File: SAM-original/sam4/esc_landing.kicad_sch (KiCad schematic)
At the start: 14 parts, among them J1 MR30PW-FB, J2 MR30PW-FB, J3 MR30PW-FB, J4 MR30PW-FB, U1 BM10B-SRSS-TB, U2 T-motor_F55A_PROII

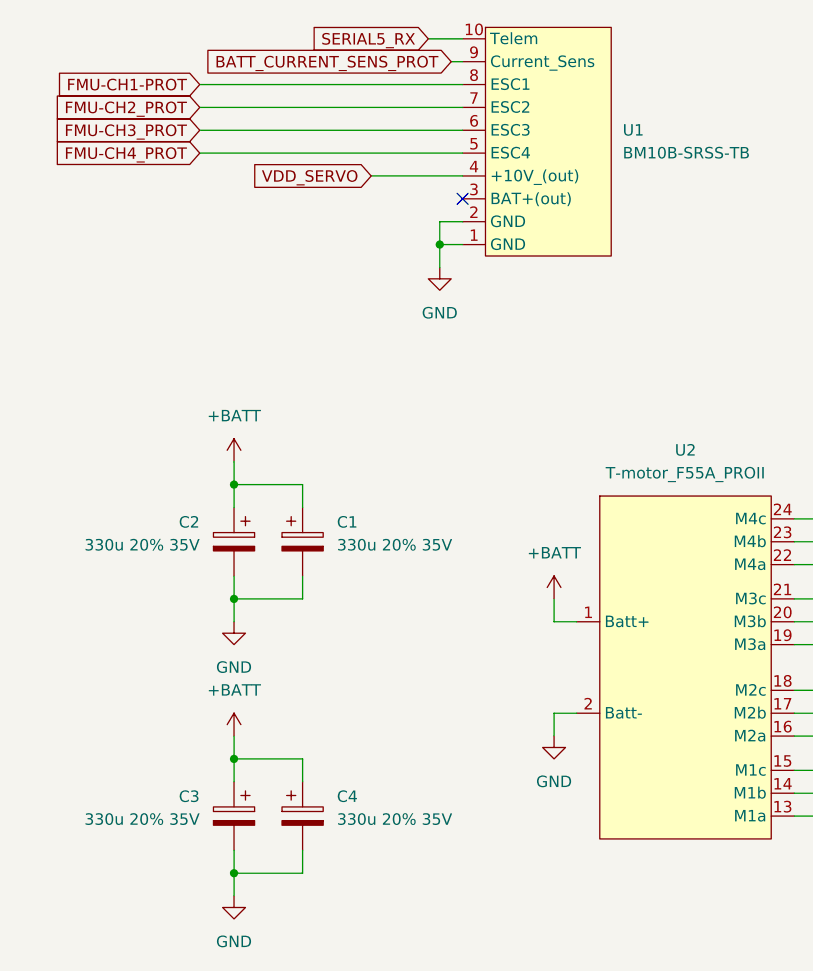
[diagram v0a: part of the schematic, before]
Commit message: reannotate sam schem to bring into parity
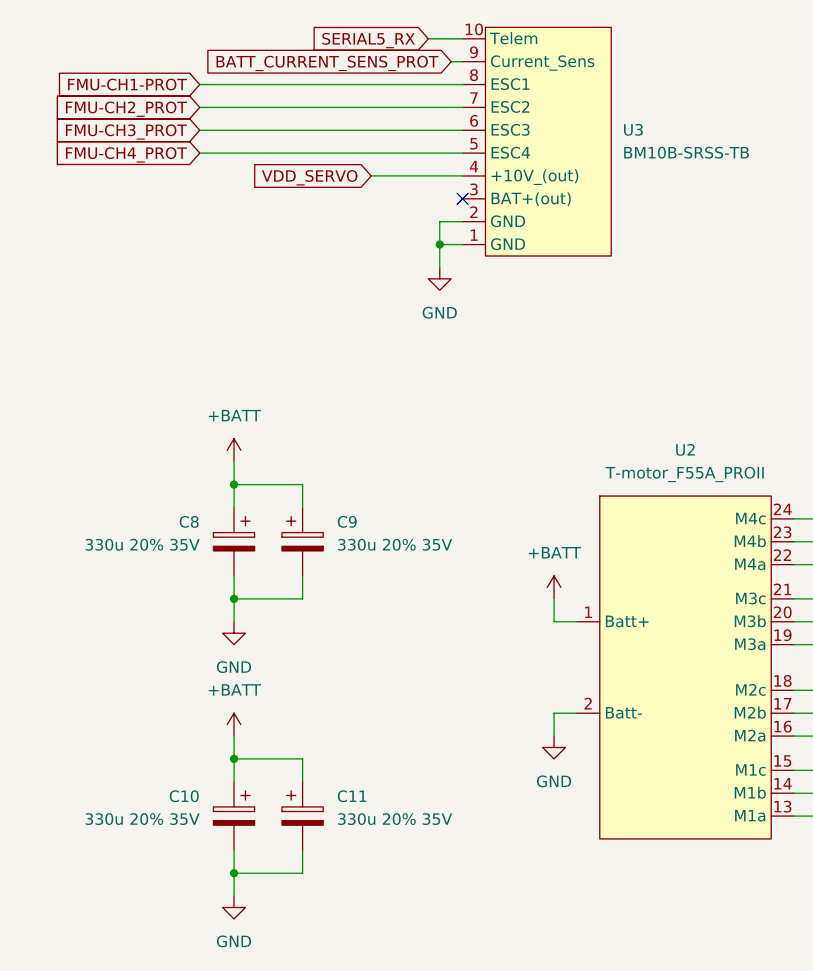
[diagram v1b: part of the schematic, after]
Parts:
- renumbered C3 to C10, C4 to C11, C2 to C8, C1 to C9, U1 to U3
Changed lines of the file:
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@@
 		(on_board yes)
 		(dnp no)
-		(property "Reference" "C3"
+		(property "Reference" "C10"
 			(at 44.45 112.1409 0)
 			(effects
@@
 			(project "sam4"
 				(path "/01aa8038-f16d-42dc-9377-7a3d64116781/45b0968d-ea93-472f-9fa5-36e57b913607"
-					(reference "C3")
+					(reference "C10")
 					(unit 1)
 				)
@@
 		(dnp no)
 		(fields_autoplaced yes)
-		(property "Reference" "C1"
+		(property "Reference" "C9"
 			(at 59.69 81.6609 0)
 			(effects
@@
 			(project ""
 				(path "/01aa8038-f16d-42dc-9377-7a3d64116781/45b0968d-ea93-472f-9fa5-36e57b913607"
-					(reference "C1")
+					(reference "C9")
 					(unit 1)
 				)
@@
 		(dnp no)
 		(fields_autoplaced yes)
-		(property "Reference" "U1"
+		(property "Reference" "U3"
 			(at 91.44 38.0999 0)
 			(effects
@@
 			(project ""
 				(path "/01aa8038-f16d-42dc-9377-7a3d64116781/45b0968d-ea93-472f-9fa5-36e57b913607"
-					(reference "U1")
+					(reference "U3")
 					(unit 1)
 				)
@@
 		(dnp no)
 		(fields_autoplaced yes)
-		(property "Reference" "C4"
+		(property "Reference" "C11"
 			(at 59.69 112.1409 0)
 			(effects
@@
 			(project "sam4"
 				(path "/01aa8038-f16d-42dc-9377-7a3d64116781/45b0968d-ea93-472f-9fa5-36e57b913607"
-					(reference "C4")
+					(reference "C11")
 					(unit 1)
 				)
@@
 		(on_board yes)
 		(dnp no)
-		(property "Reference" "C2"
+		(property "Reference" "C8"
 			(at 44.45 81.6609 0)
 			(effects
@@
 			(project "sam4"
 				(path "/01aa8038-f16d-42dc-9377-7a3d64116781/45b0968d-ea93-472f-9fa5-36e57b913607"
-					(reference "C2")
-					(unit 1)
-				)
+					(reference "C8")
+					(unit 1)
+				)

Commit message: place top. revisit missing parts
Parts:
- renumbered J1 to M1, J2 to M2, J3 to M3, J4 to M4
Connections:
- net M1a: now also M4.1 (Pin_1); no longer M4.3 (Pin_3)
- net M1c: now also M4.3 (Pin_3); no longer M4.1 (Pin_1)
- net M2a: now also M3.1 (Pin_1); no longer M3.3 (Pin_3)
- net M2c: now also M3.3 (Pin_3); no longer M3.1 (Pin_1)
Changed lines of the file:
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@@
 		(lib_id "Connector:Conn_01x03_Socket")
 		(at 130.81 111.76 0)
-		(unit 1)
-		(exclude_from_sim no)
-		(in_bom yes)
-		(on_board yes)
-		(dnp no)
-		(fields_autoplaced yes)
-		(property "Reference" "J4"
-			(at 132.08 110.4899 0)
+		(mirror x)
+		(unit 1)
+		(exclude_from_sim no)
+		(in_bom yes)
+		(on_board yes)
+		(dnp no)
+		(property "Reference" "M4"
+			(at 132.08 113.0301 0)
 			(effects
 				(font
@@
 		)
 		(property "Value" "MR30PW-FB"
-			(at 132.08 113.0299 0)
+			(at 132.08 110.4901 0)
 			(effects
 				(font
@@
 			(project "sam4"
 				(path "/01aa8038-f16d-42dc-9377-7a3d64116781/45b0968d-ea93-472f-9fa5-36e57b913607"
-					(reference "J4")
+					(reference "M4")
 					(unit 1)
 				)
@@
 		(dnp no)
 		(fields_autoplaced yes)
-		(property "Reference" "J1"
+		(property "Reference" "M1"
 			(at 132.08 82.5499 0)
 			(effects
@@
 			(project ""
 				(path "/01aa8038-f16d-42dc-9377-7a3d64116781/45b0968d-ea93-472f-9fa5-36e57b913607"
-					(reference "J1")
+					(reference "M1")
 					(unit 1)
 				)
@@
 		(lib_id "Connector:Conn_01x03_Socket")
 		(at 130.81 102.87 0)
-		(unit 1)
-		(exclude_from_sim no)
-		(in_bom yes)
-		(on_board yes)
-		(dnp no)
-		(fields_autoplaced yes)
-		(property "Reference" "J3"
-			(at 132.08 101.5999 0)
+		(mirror x)
+		(unit 1)
+		(exclude_from_sim no)
+		(in_bom yes)
+		(on_board yes)
+		(dnp no)
+		(property "Reference" "M3"
+			(at 132.08 104.1401 0)
 			(effects
 				(font
@@
 		)
 		(property "Value" "MR30PW-FB"
-			(at 132.08 104.1399 0)
+			(at 132.08 101.6001 0)
 			(effects
 				(font
@@
 			(project "sam4"
 				(path "/01aa8038-f16d-42dc-9377-7a3d64116781/45b0968d-ea93-472f-9fa5-36e57b913607"
-					(reference "J3")
+					(reference "M3")
 					(unit 1)
 				)
@@
 		(dnp no)
 		(fields_autoplaced yes)
-		(property "Reference" "J2"
+		(property "Reference" "M2"
 			(at 132.08 91.4399 0)
 			(effects
@@
 			(project "sam4"
 				(path "/01aa8038-f16d-42dc-9377-7a3d64116781/45b0968d-ea93-472f-9fa5-36e57b913607"
-					(reference "J2")
-					(unit 1)
-				)
+					(reference "M2")
+					(unit 1)
+				)

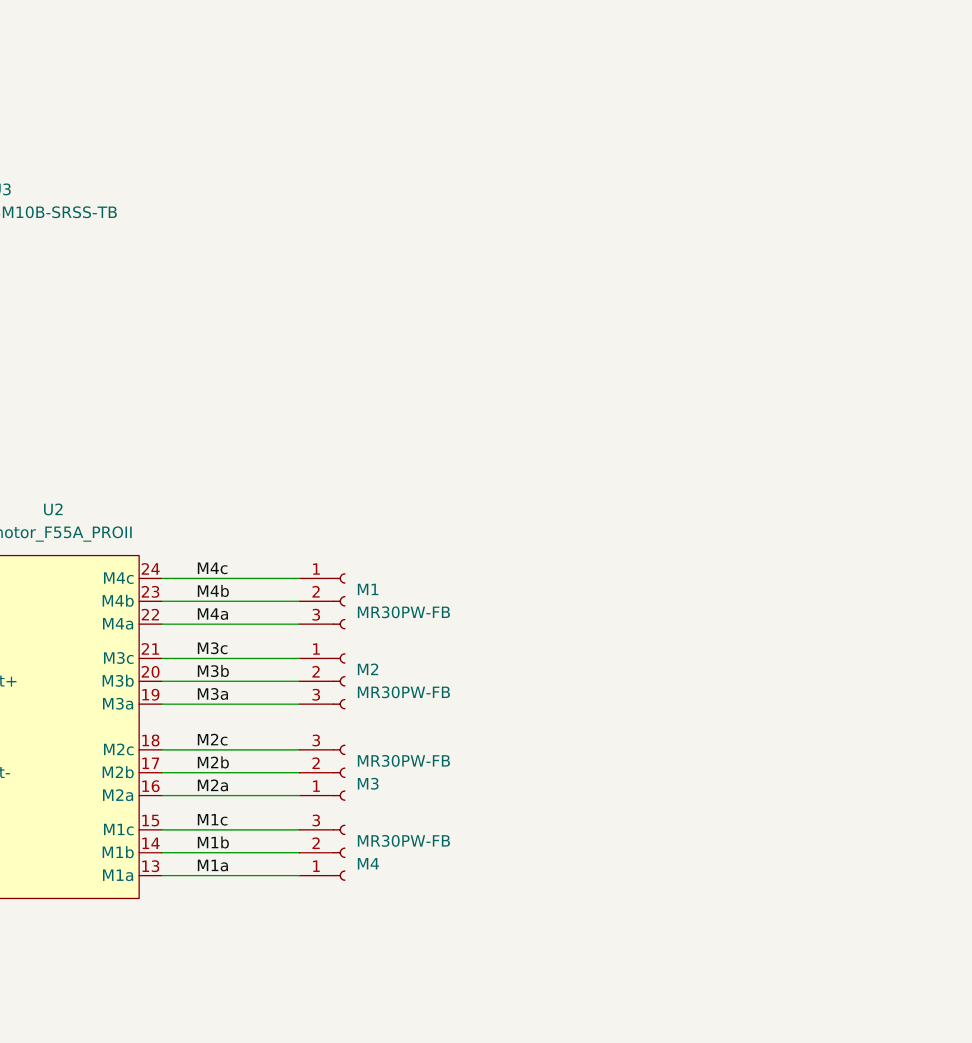
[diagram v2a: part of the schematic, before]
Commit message: finalize core routing
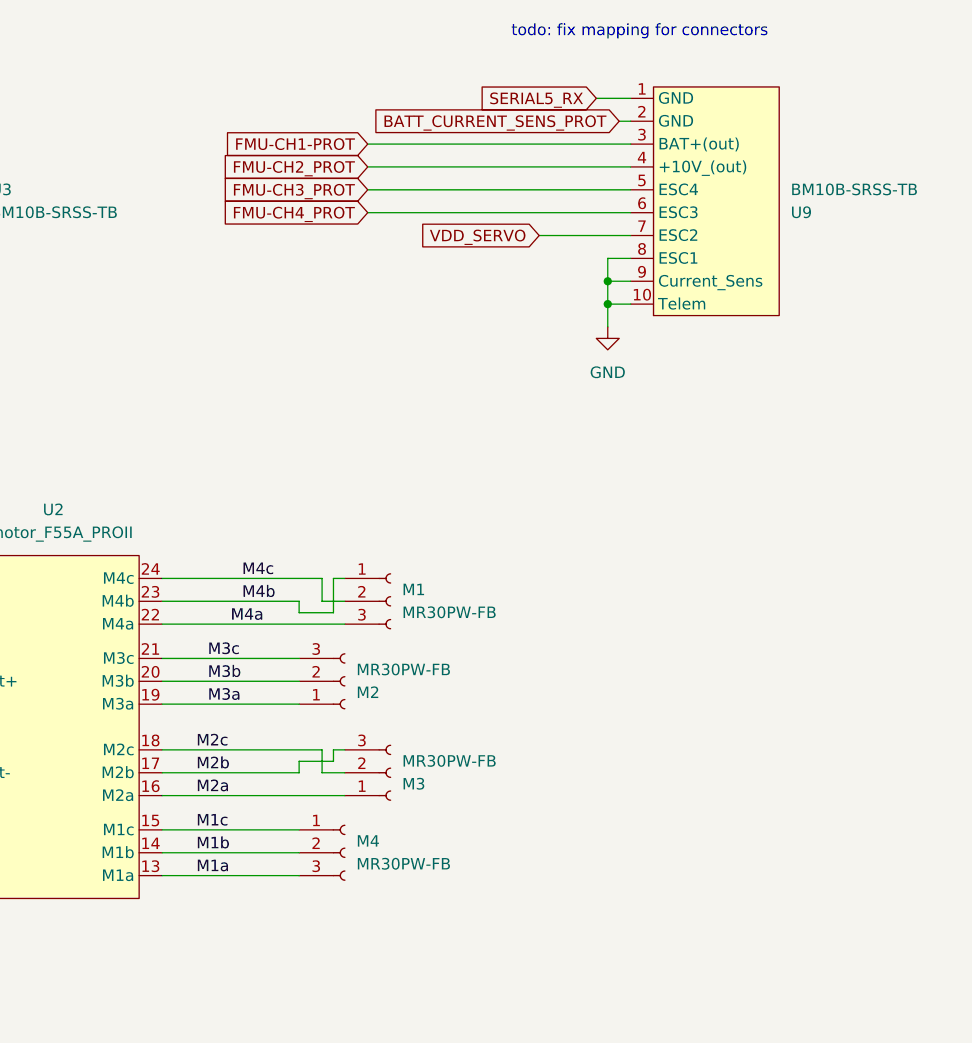
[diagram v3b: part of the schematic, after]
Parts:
- added U9: BM10B-SRSS-TB, Connector_JST:JST_GH_BM08B-GHS-TBT_1x08-1MP_P1.25mm_Vertical, symbol aerpaw-symbols:BM10B-SRSS-TB
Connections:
- net BATT_CURRENT_SENS_PROT: now also U9.2 (GND)
- net FMU-CH1-PROT: now also U9.3 (BAT+(out))
- net FMU-CH2_PROT: now also U9.4 (+10V_(out))
- net FMU-CH3_PROT: now also U9.5 (ESC4)
- net FMU-CH4_PROT: now also U9.6 (ESC3)
- net GND: now also U9.10 (Telem), U9.8 (ESC1), U9.9 (Current_Sens)
- net M1a: now also M4.3 (Pin_3); no longer M4.1 (Pin_1)
- net M1c: now also M4.1 (Pin_1); no longer M4.3 (Pin_3)
- net M2b: now also M3.3 (Pin_3); no longer M3.2 (Pin_2)
- net M2c: now also M3.2 (Pin_2); no longer M3.3 (Pin_3)
- net M3a: now also M2.1 (Pin_1); no longer M2.3 (Pin_3)
- net M3c: now also M2.3 (Pin_3); no longer M2.1 (Pin_1)
- net M4b: now also M1.1 (Pin_1); no longer M1.2 (Pin_2)
- net M4c: now also M1.2 (Pin_2); no longer M1.1 (Pin_1)
- net SERIAL5_RX: now also U9.1 (GND)
- net VDD_SERVO: now also U9.7 (ESC2)
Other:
- note added: "todo: fix mapping for connectors"
- moved on the sheet: M1, M3

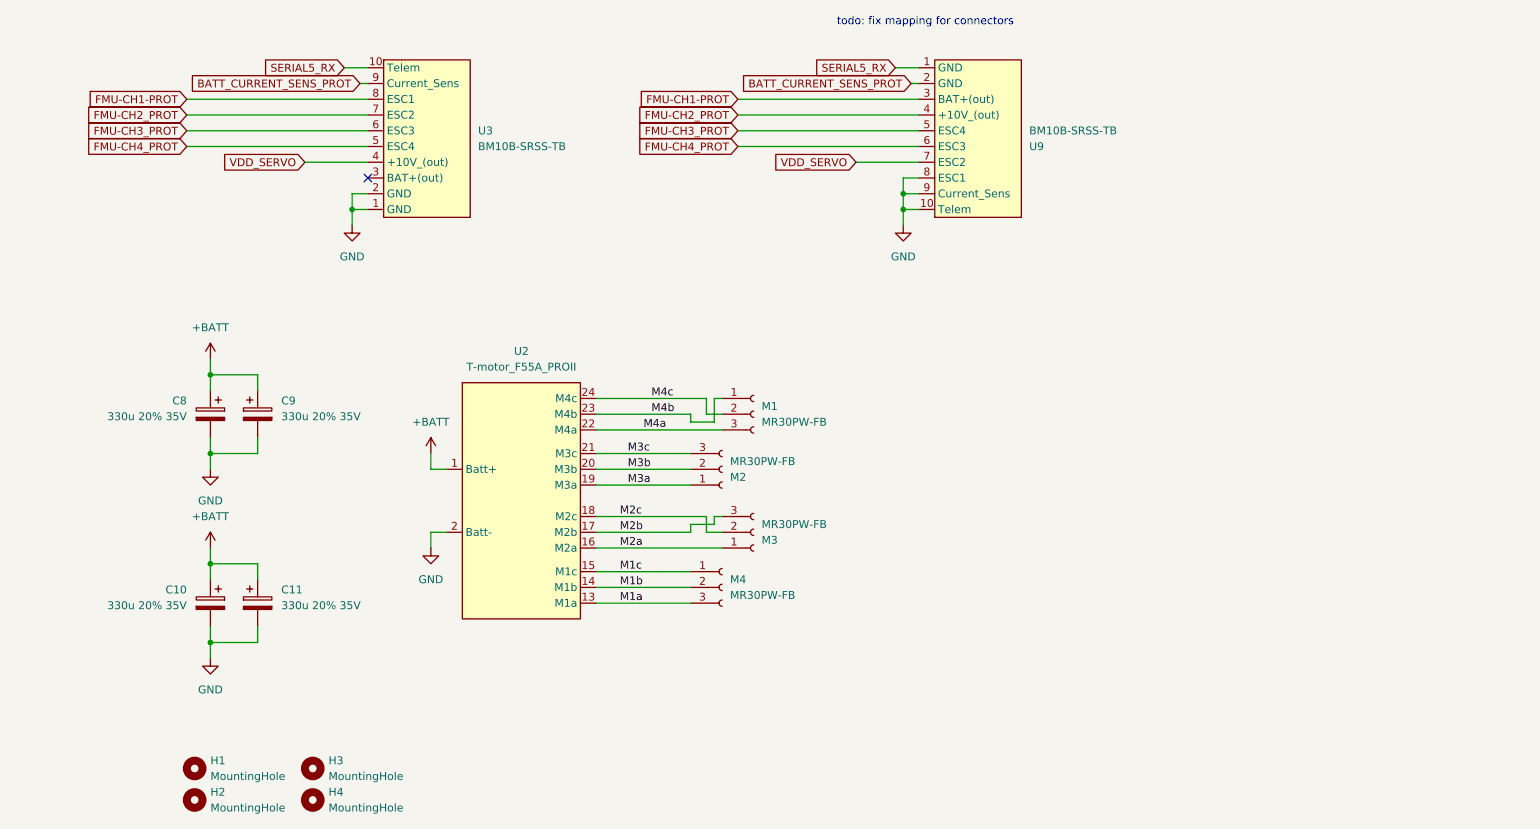
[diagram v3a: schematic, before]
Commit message: add updated SAM4 routing (DRC clean) + model
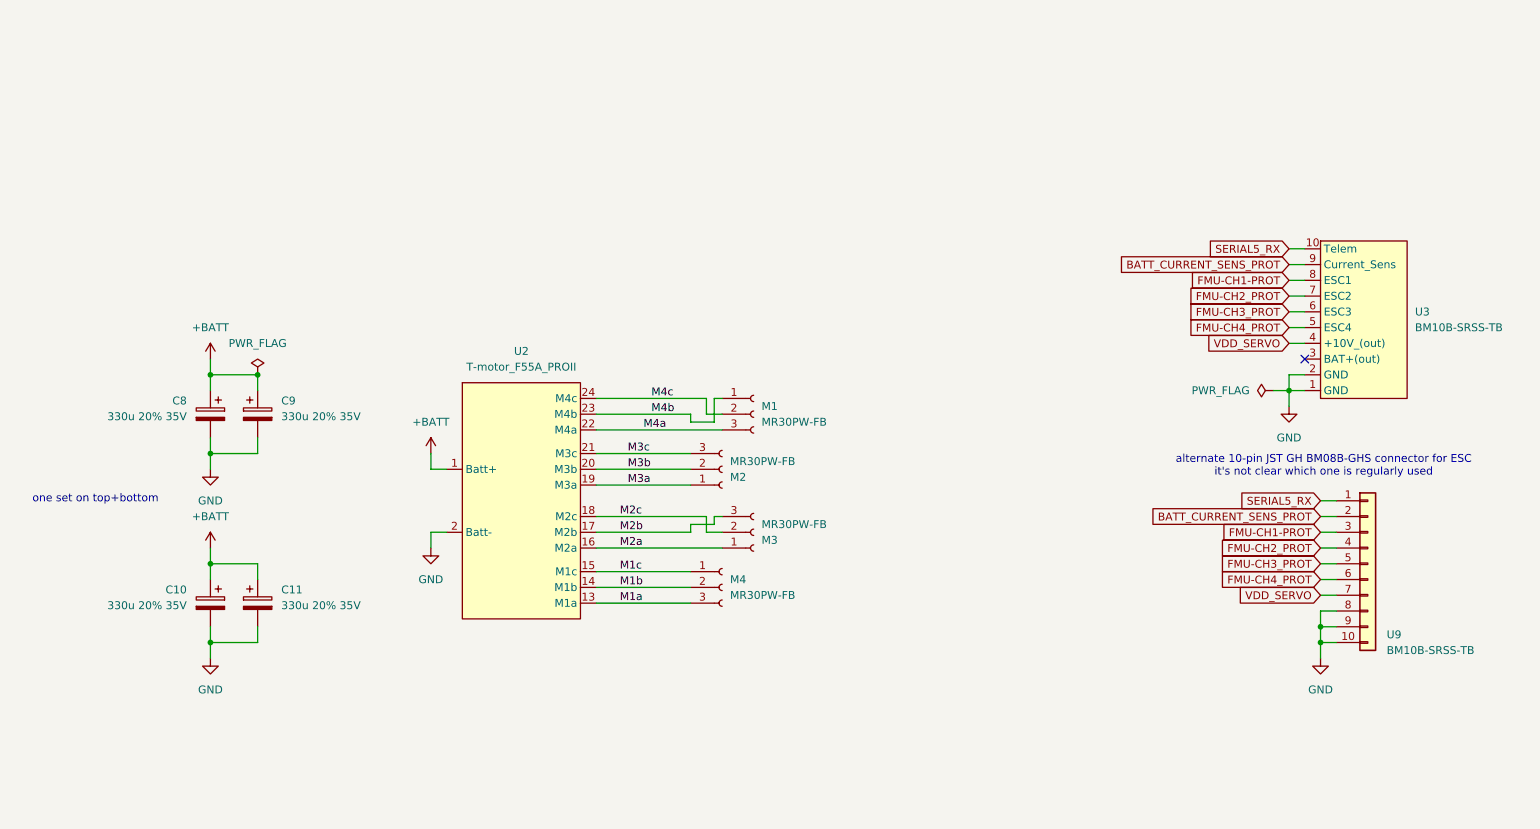
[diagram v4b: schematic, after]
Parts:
- removed H1, H2, H3, H4: MountingHole, MountingHole:MountingHole_3.2mm_M3_DIN965, symbol Mechanical:MountingHole
- M1, M2, M3, M4: LCSC (none) -> C19268035
- U3: LCSC (none) -> C265443
- U9: symbol aerpaw-symbols:BM10B-SRSS-TB -> Connector_Generic:Conn_01x10; LCSC (none) -> C133062
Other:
- note added: "alternate 10-pin JST GH BM08B-GHS connector for ESC it's not clear which one is regularly used"
- note added: "one set on top+bottom"
- note removed: "todo: fix mapping for connectors"
- moved on the sheet: U3, U9
